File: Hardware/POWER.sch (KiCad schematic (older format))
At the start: 25 parts, among them P1 RCA_conn_x2, P2 +12V, P3 3.5mm_conn_tip_switch, P4 3.5mm_conn_tip_switch, P43 +5V, P44 +12V_AUX, P45 +5V_AUX, Q2 BSS138, SW1 PWR_BTN, U2 LP38692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

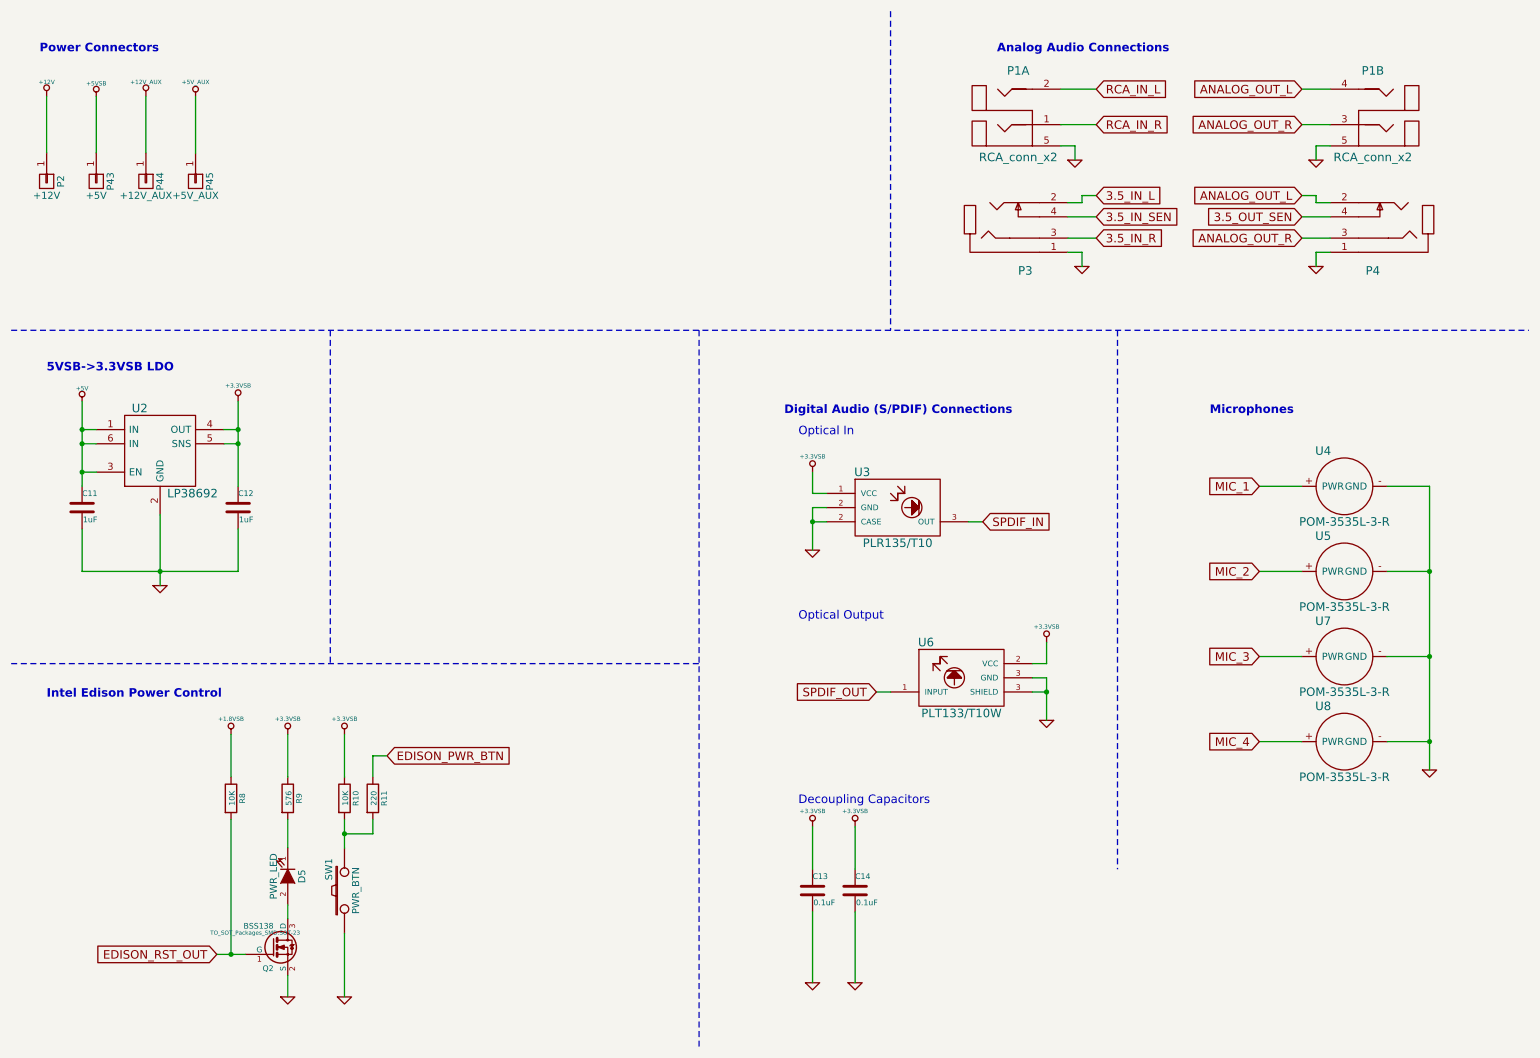
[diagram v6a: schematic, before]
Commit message: Digital Half completed placement
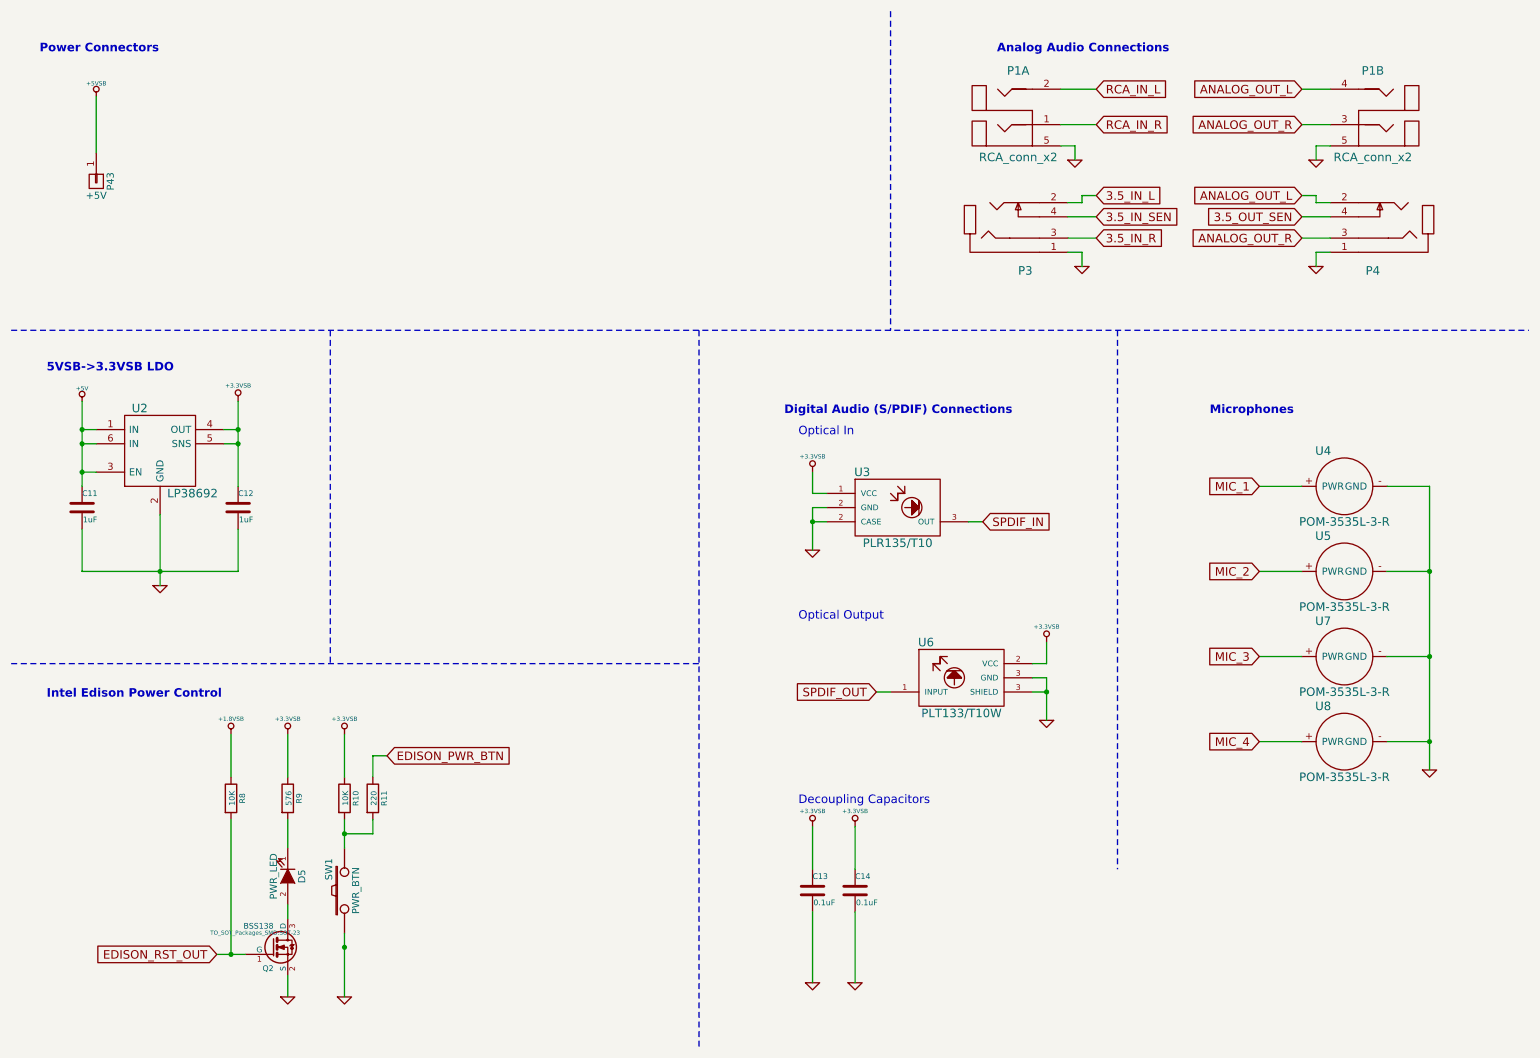
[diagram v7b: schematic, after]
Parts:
- removed P2: +12V, Pin_Headers:Pin_Header_Straight_1x01, symbol CONN_01X01
- removed P44: +12V_AUX, Pin_Headers:Pin_Header_Straight_1x01, symbol CONN_01X01
- removed P45: +5V_AUX, Pin_Headers:Pin_Header_Straight_1x01, symbol CONN_01X01
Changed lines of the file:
@@
 	2050 6200 2050 7150
 Wire Wire Line
-	2850 7450 2850 7000
+	2850 7000 2850 7100
+Wire Wire Line
+	2850 7100 2850 7450
 Wire Wire Line
 	2850 5600 2850 5900
 Connection ~ 2850 6300
 Wire Wire Line
-	2850 6200 2850 6400
+	2850 6200 2850 6300
+Wire Wire Line
+	2850 6300 2850 6400
 $Comp
 L R-RESCUE-museV2 R11
@@
 $EndComp
 Wire Wire Line
-	3050 6300 2850 6300
+	2850 6300 3050 6300
 $Comp
 L +3.3VSB #PWR018
@@
 5VSB->3.3VSB LDO
 Wire Wire Line
-	1000 3250 1000 3850
+	1000 3250 1000 3450
+Wire Wire Line
+	1000 3450 1000 3550
+Wire Wire Line
+	1000 3550 1000 3750
+Wire Wire Line
+	1000 3750 1000 3850
 Wire Wire Line
 	1000 3550 1100 3550
@@
 Connection ~ 1000 3450
 Wire Wire Line
-	1550 4050 1550 4550
-Wire Wire Line
-	2100 3250 2100 3850
+	1550 4050 1550 4450
+Wire Wire Line
+	1550 4450 1550 4550
+Wire Wire Line
+	2100 3250 2100 3450
+Wire Wire Line
+	2100 3450 2100 3550
+Wire Wire Line
+	2100 3550 2100 3850
 Connection ~ 1000 3550
 Wire Wire Line
 	1000 4150 1000 4450
 Wire Wire Line
-	1000 4450 2100 4450
+	1000 4450 1550 4450
+Wire Wire Line
+	1550 4450 2100 4450
 Connection ~ 1550 4450
 Wire Wire Line
@@
 	2000 3450 2100 3450
 Connection ~ 2100 3450
-$Comp
-L +12V #PWR021
-U 1 1 57EB439D
-P 750 1100
-F 0 "#PWR021" H 750 1050 20  0001 C CNN
-F 1 "+12V" H 750 1200 30  0000 C CNN
-F 2 "" H 750 1100 60  0000 C CNN
-F 3 "" H 750 1100 60  0000 C CNN
-	1    750  1100
-	1    0    0    -1
-$EndComp
 Text Notes 700  800  0    60   ~ 12
 Power Connectors
-$Comp
-L +12V_AUX #PWR022
-U 1 1 57EB43C6
-P 1450 1100
-F 0 "#PWR022" H 1450 1050 20  0001 C CNN
-F 1 "+12V_AUX" H 1450 1200 30  0000 C CNN
-F 2 "" H 1450 1100 60  0000 C CNN
-F 3 "" H 1450 1100 60  0000 C CNN
-	1    1450 1100
-	1    0    0    -1
-$EndComp
-$Comp
-L +5V_AUX #PWR023
-U 1 1 57EB43D0
-P 1800 1100
-F 0 "#PWR023" H 1800 1190 20  0001 C CNN
-F 1 "+5V_AUX" H 1800 1200 30  0000 C CNN
-F 2 "" H 1800 1100 60  0000 C CNN
-F 3 "" H 1800 1100 60  0000 C CNN
-	1    1800 1100
-	1    0    0    -1
-$EndComp
 Text GLabel 3150 5750 2    60   Input ~ 0
 EDISON_PWR_BTN
@@
 EDISON_RST_OUT
 Wire Wire Line
-	1950 7150 2150 7150
+	1950 7150 2050 7150
+Wire Wire Line
+	2050 7150 2150 7150
 Wire Notes Line
 	5350 2750 5350 7800
@@
 Optical In
 $Comp
-L +3.3VSB #PWR024
+L +3.3VSB #PWR021
 U 1 1 57F7D788
 P 7800 4950
-F 0 "#PWR024" H 7800 4910 30  0001 C CNN
+F 0 "#PWR021" H 7800 4910 30  0001 C CNN
 F 1 "+3.3VSB" H 7800 5060 30  0000 C CNN
 F 2 "" H 7800 4950 60  0000 C CNN
@@
 $EndComp
 $Comp
-L GND-RESCUE-museV2-RESCUE-museV2 #PWR025
+L GND-RESCUE-museV2-RESCUE-museV2 #PWR022
 U 1 1 57F7D78E
 P 7800 5500
-F 0 "#PWR025" H 7800 5500 30  0001 C CNN
+F 0 "#PWR022" H 7800 5500 30  0001 C CNN
 F 1 "GND" H 7800 5430 30  0001 C CNN
 F 2 "" H 7800 5500 60  0000 C CNN
@@
 $EndComp
 $Comp
-L GND-RESCUE-museV2-RESCUE-museV2 #PWR026
+L GND-RESCUE-museV2-RESCUE-museV2 #PWR023
 U 1 1 57F7D796
 P 6150 4300
-F 0 "#PWR026" H 6150 4300 30  0001 C CNN
+F 0 "#PWR023" H 6150 4300 30  0001 C CNN
 F 1 "GND" H 6150 4230 30  0001 C CNN
 F 2 "" H 6150 4300 60  0000 C CNN
@@
 $EndComp
 $Comp
-L +3.3VSB #PWR027
+L +3.3VSB #PWR024
 U 1 1 57F7D79C
 P 6150 3750
-F 0 "#PWR027" H 6150 3710 30  0001 C CNN
+F 0 "#PWR024" H 6150 3710 30  0001 C CNN
 F 1 "+3.3VSB" H 6150 3860 30  0000 C CNN
 F 2 "" H 6150 3750 60  0000 C CNN
@@
 Analog Audio Connections
 $Comp
-L GND-RESCUE-museV2-RESCUE-museV2 #PWR028
+L GND-RESCUE-museV2-RESCUE-museV2 #PWR025
 U 1 1 57F7D7C3
 P 8050 2300
-F 0 "#PWR028" H 8050 2300 30  0001 C CNN
+F 0 "#PWR025" H 8050 2300 30  0001 C CNN
 F 1 "GND" H 8050 2230 30  0001 C CNN
 F 2 "" H 8050 2300 60  0000 C CNN
@@
 $EndComp
 $Comp
-L GND-RESCUE-museV2-RESCUE-museV2 #PWR029
+L GND-RESCUE-museV2-RESCUE-museV2 #PWR026
 U 1 1 57F7D7D4
 P 9700 2300
-F 0 "#PWR029" H 9700 2300 30  0001 C CNN
+F 0 "#PWR026" H 9700 2300 30  0001 C CNN
 F 1 "GND" H 9700 2230 30  0001 C CNN
 F 2 "" H 9700 2300 60  0000 C CNN
@@
 $EndComp
 $Comp
-L GND-RESCUE-museV2-RESCUE-museV2 #PWR030
+L GND-RESCUE-museV2-RESCUE-museV2 #PWR027
 U 1 1 57F7D80B
 P 10500 5850
-F 0 "#PWR030" H 10500 5850 30  0001 C CNN
+F 0 "#PWR027" H 10500 5850 30  0001 C CNN
 F 1 "GND" H 10500 5780 30  0001 C CNN
 F 2 "" H 10500 5850 60  0000 C CNN
@@
 Connection ~ 10500 4450
 Wire Wire Line
-	10500 3850 10500 5850
+	10500 3850 10500 4450
+Wire Wire Line
+	10500 4450 10500 5050
+Wire Wire Line
+	10500 5050 10500 5650
+Wire Wire Line
+	10500 5650 10500 5850
 Wire Wire Line
 	10200 3850 10500 3850
@@
 	6150 3900 6250 3900
 Wire Wire Line
-	6150 4000 6150 4300
+	6150 4000 6150 4100
+Wire Wire Line
+	6150 4100 6150 4300
 Wire Wire Line
 	6150 4000 6250 4000
@@
 Connection ~ 6150 4100
 Wire Wire Line
-	7800 5200 7800 5500
+	7800 5200 7800 5300
+Wire Wire Line
+	7800 5300 7800 5500
 Wire Wire Line
 	7800 5200 7700 5200
@@
 MIC_4
 $Comp
-L GND-RESCUE-museV2-RESCUE-museV2 #PWR031
+L GND-RESCUE-museV2-RESCUE-museV2 #PWR028
 U 1 1 57FA222D
 P 6450 7350
-F 0 "#PWR031" H 6450 7350 30  0001 C CNN
+F 0 "#PWR028" H 6450 7350 30  0001 C CNN
 F 1 "GND" H 6450 7280 30  0001 C CNN
 F 2 "" H 6450 7350 60  0000 C CNN
@@
 $EndComp
 $Comp
-L +3.3VSB #PWR032
+L +3.3VSB #PWR029
 U 1 1 57FA223A
 P 6450 6250
-F 0 "#PWR032" H 6450 6210 30  0001 C CNN
+F 0 "#PWR029" H 6450 6210 30  0001 C CNN
 F 1 "+3.3VSB" H 6450 6360 30  0000 C CNN
 F 2 "" H 6450 6250 60  0000 C CNN
@@
 $EndComp
 $Comp
-L GND-RESCUE-museV2-RESCUE-museV2 #PWR033
+L GND-RESCUE-museV2-RESCUE-museV2 #PWR030
 U 1 1 57FA2240
 P 6150 7350
-F 0 "#PWR033" H 6150 7350 30  0001 C CNN
+F 0 "#PWR030" H 6150 7350 30  0001 C CNN
 F 1 "GND" H 6150 7280 30  0001 C CNN
 F 2 "" H 6150 7350 60  0000 C CNN
@@
 $EndComp
 $Comp
-L +3.3VSB #PWR034
+L +3.3VSB #PWR031
 U 1 1 57FA224D
 P 6150 6250
-F 0 "#PWR034" H 6150 6210 30  0001 C CNN
+F 0 "#PWR031" H 6150 6210 30  0001 C CNN
 F 1 "+3.3VSB" H 6150 6360 30  0000 C CNN
 F 2 "" H 6150 6250 60  0000 C CNN
@@
 	1100 3750 1000 3750
 Connection ~ 1000 3750
-$Comp
-L CONN_01X01 P2
-U 1 1 5858BA7C
-P 750 1700
-F 0 "P2" H 750 1800 50  0000 C CNN
-F 1 "+12V" V 850 1700 50  0000 C CNN
-F 2 "Pin_Headers:Pin_Header_Straight_1x01" H 750 1700 60  0001 C CNN
-F 3 "" H 750 1700 60  0000 C CNN
-	1    750  1700
-	0    1    1    0
-$EndComp
 $Comp
 L CONN_01X01 P43
@@
 	0    1    1    0
 $EndComp
-$Comp
-L CONN_01X01 P44
-U 1 1 5858BD2E
-P 1450 1700
-F 0 "P44" H 1450 1800 50  0000 C CNN
-F 1 "+12V_AUX" V 1550 1700 50  0000 C CNN
-F 2 "Pin_Headers:Pin_Header_Straight_1x01" H 1450 1700 60  0001 C CNN
-F 3 "" H 1450 1700 60  0000 C CNN
-	1    1450 1700
-	0    1    1    0
-$EndComp
-$Comp
-L CONN_01X01 P45
-U 1 1 5858BD35
-P 1800 1700
-F 0 "P45" H 1800 1800 50  0000 C CNN
-F 1 "+5V_AUX" V 1900 1700 50  0000 C CNN
-F 2 "Pin_Headers:Pin_Header_Straight_1x01" H 1800 1700 60  0001 C CNN
-F 3 "" H 1800 1700 60  0000 C CNN
-	1    1800 1700
-	0    1    1    0
-$EndComp
-Wire Wire Line
-	750  1100 750  1500
 Wire Wire Line
 	1100 1500 1100 1100
-Wire Wire Line
-	1450 1100 1450 1500
-Wire Wire Line
-	1800 1100 1800 1500
-$Comp
-L +5VSB #PWR035
+$Comp
+L +5VSB #PWR032
 U 1 1 5859E2FF
 P 1100 1100
-F 0 "#PWR035" H 1100 1190 20  0001 C CNN
+F 0 "#PWR032" H 1100 1190 20  0001 C CNN
 F 1 "+5VSB" H 1100 1190 30  0000 C CNN
 F 2 "" H 1100 1100 60  0000 C CNN
@@
 	9600 1300 9800 1300
 $Comp
-L GND-RESCUE-museV2-RESCUE-museV2 #PWR036
+L GND-RESCUE-museV2-RESCUE-museV2 #PWR033
 U 1 1 585AD273
 P 9700 1550
-F 0 "#PWR036" H 9700 1550 30  0001 C CNN
+F 0 "#PWR033" H 9700 1550 30  0001 C CNN
 F 1 "GND" H 9700 1480 30  0001 C CNN
 F 2 "" H 9700 1550 60  0000 C CNN
@@
 	9700 1550 9700 1450
 $Comp
-L GND-RESCUE-museV2-RESCUE-museV2 #PWR037
+L GND-RESCUE-museV2-RESCUE-museV2 #PWR034
 U 1 1 585AD9C8
 P 8000 1550
-F 0 "#PWR037" H 8000 1550 30  0001 C CNN
+F 0 "#PWR034" H 8000 1550 30  0001 C CNN
 F 1 "GND" H 8000 1480 30  0001 C CNN
 F 2 "" H 8000 1550 60  0000 C CNN
@@
 	8000 1450 7900 1450
 $Comp
-L +5V #PWR038
+L +5V #PWR035
 U 1 1 58627E51
 P 1000 3250
-F 0 "#PWR038" H 1000 3340 20  0001 C CNN
+F 0 "#PWR035" H 1000 3340 20  0001 C CNN
 F 1 "+5V" H 1000 3340 30  0000 C CNN
 F 2 "" H 1000 3250 60  0000 C CNN
@@
 	1    0    0    -1
 $EndComp
+Connection ~ 2850 7100
 $EndSCHEMATC

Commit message: Beginning analog chip placement
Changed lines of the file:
@@
 	2050 6200 2050 7150
 Wire Wire Line
-	2850 7000 2850 7100
-Wire Wire Line
-	2850 7100 2850 7450
+	2850 7000 2850 7450
 Wire Wire Line
 	2850 5600 2850 5900
 Connection ~ 2850 6300
 Wire Wire Line
-	2850 6200 2850 6300
-Wire Wire Line
-	2850 6300 2850 6400
+	2850 6200 2850 6400
 $Comp
 L R-RESCUE-museV2 R11
@@
 $EndComp
 Wire Wire Line
-	3050 6200 3050 6300
+	3050 6300 3050 6200
 Wire Wire Line
 	3050 5750 3050 5900
@@
 5VSB->3.3VSB LDO
 Wire Wire Line
-	1000 3250 1000 3450
-Wire Wire Line
-	1000 3450 1000 3550
-Wire Wire Line
-	1000 3550 1000 3750
-Wire Wire Line
-	1000 3750 1000 3850
+	1000 3250 1000 3850
 Wire Wire Line
 	1000 3550 1100 3550
@@
 Connection ~ 1000 3450
 Wire Wire Line
-	1550 4050 1550 4450
-Wire Wire Line
-	1550 4450 1550 4550
-Wire Wire Line
-	2100 3250 2100 3450
-Wire Wire Line
-	2100 3450 2100 3550
-Wire Wire Line
-	2100 3550 2100 3850
+	1550 4050 1550 4550
+Wire Wire Line
+	2100 3250 2100 3850
 Connection ~ 1000 3550
 Wire Wire Line
 	1000 4150 1000 4450
 Wire Wire Line
-	1000 4450 1550 4450
-Wire Wire Line
-	1550 4450 2100 4450
+	1000 4450 2100 4450
 Connection ~ 1550 4450
 Wire Wire Line
@@
 EDISON_RST_OUT
 Wire Wire Line
-	1950 7150 2050 7150
-Wire Wire Line
-	2050 7150 2150 7150
+	1950 7150 2150 7150
 Wire Notes Line
 	5350 2750 5350 7800
@@
 Connection ~ 10500 4450
 Wire Wire Line
-	10500 3850 10500 4450
-Wire Wire Line
-	10500 4450 10500 5050
-Wire Wire Line
-	10500 5050 10500 5650
-Wire Wire Line
-	10500 5650 10500 5850
+	10500 3850 10500 5850
 Wire Wire Line
 	10200 3850 10500 3850
@@
 	6150 3900 6250 3900
 Wire Wire Line
-	6150 4000 6150 4100
-Wire Wire Line
-	6150 4100 6150 4300
+	6150 4000 6150 4300
 Wire Wire Line
 	6150 4000 6250 4000
@@
 Connection ~ 6150 4100
 Wire Wire Line
-	7800 5200 7800 5300
-Wire Wire Line
-	7800 5300 7800 5500
+	7800 5200 7800 5500
 Wire Wire Line
 	7800 5200 7700 5200
